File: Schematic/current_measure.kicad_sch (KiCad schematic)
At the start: 14 parts, among them J1 Conn_02x03_Counter_Clockwise, J2 Screw_Terminal_01x02, SW1 SW_Push, U1 STM32G4A1KEUx, U2 LM4040DBZ-2.0, U3 INA186

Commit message: Week 27.10.2025
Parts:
- removed U2: LM4040DBZ-2.0, Package_TO_SOT_SMD:SOT-23, symbol Reference_Voltage:LM4040DBZ-2.0
- removed U3: INA186, Package_TO_SOT_SMD:SOT-23-5_HandSoldering, symbol Amplifier_Current:INA180A1
- added C10: 10n, symbol Device:C
- added C11, C12, C13: 100n, symbol Device:C
- added C14: 1u, symbol Device:C
- added C15: 10u, symbol Device:C
- added C16: 0.1u, symbol Device:C
- added C17, C5: C, symbol Device:C
- added C6, C7: 0.1µ, symbol Device:C
- added C8: 4.7µ, symbol Device:C
- added C9: 10µ, symbol Device:C
- added J3: Conn_01x04_Pin, Connector_PinHeader_2.54mm:PinHeader_1x04_P2.54mm_Vertical, symbol Connector:Conn_01x04_Pin
- added J4: Conn_01x02, Connector_PinHeader_2.54mm:PinHeader_1x02_P2.54mm_Vertical, symbol Connector_Generic:Conn_01x02
- added R10: 220, symbol Device:R
- added R11: 49.9, symbol Device:R
- added R12: 910, symbol Device:R
- added R13: 100, symbol Device:R
- added R14, R7: 10, symbol Device:R
- added R5: 10k, symbol Device:R
- added R6: 1k, symbol Device:R
- added R8: 820k, symbol Device:R
- added R9: 499, symbol Device:R
- added U2: INA186, Package_TO_SOT_SMD:SOT-363_SC-70-6_Handsoldering, symbol Amplifier_Current:INA199xxDCK
- added U3: MCP6001-OT, Package_SO:SOIC-8_3.9x4.9mm_P1.27mm, symbol Amplifier_Operational:MCP6001-OT
- added U4: OPA350, Package_SO:SOIC-8_3.9x4.9mm_P1.27mm, symbol Amplifier_Operational:OPA356xxD
- added U5, U6: 6N137, Package_DIP:DIP-8_W7.62mm, symbol Isolator:6N137
- added U7: MIC5365-3.3YD5, Package_TO_SOT_SMD:TSOT-23-5_HandSoldering, symbol Regulator_Linear:MIC5365-3.3YD5
- C1: value 470n -> 22n
- C2: value C -> 0.1u
- C3: value C -> 4.7u
- C4: value C -> 10u
- R1: value 100 -> 9.1k; footprint Resistor_SMD:R_0805_2012Metric_Pad1.20x1.40mm_HandSolder -> (none)
- R3, R4: value 100 -> 1k
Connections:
- net +3.3V: now also C12.1, C7.1, C8.1, C9.1, U2.3 (V+), U3.2 (V-), U4.7 (V+), U6.8 (VCC), U7.5 (VOUT); no longer R1.1
- net Current_measure: now also C17.1, R14.2, R6.1
- net GND: now also SW1.1, C10.2, C12.2, C13.2, C14.2, C15.2, C16.2, C17.2, C5.2, C6.2, C7.2, C8.2, C9.2, J4.1 (Pin_1), R11.2, R12.2, U2.2 (GND), U3.5 (V+), U4.4 (V-), U6.5 (GND), U7.2 (GND)
- net ~{RESET}: now also SW1.2, C5.1
- net at C1.1, R3.2: now also U2.4 (+)
- net at C1.2, R4.2: now also U2.5 (-)
- net at R1.2: now also R12.1, U3.3 (+)
- new net: R5.2, R7.2, U4.6
- new net: C14.1, C15.1, C16.1, J4.2 (Pin_2), R13.1, U7.1 (VIN)
- new net: C13.1, R13.2, U7.3 (EN)
- new net: R5.1, R6.2, U4.3 (+)
- new net: R11.1, R8.2, R9.2, U4.2 (-)
- new net: R14.1, U2.6
- new net: U2.1 (REF), U3.1, U3.4 (-)
- new net: C10.1, C11.1, R10.2
- new net ADC_in: C6.1, R7.1
- new net DAC_ref_{offset}: R1.1
- new net DAC_{offset}: R9.1
- new net Trig: C11.2, R8.1
- new net Trig_{gen}: R10.1
- new net USB_+5: J3.4 (Pin_4), U5.8 (VCC)
- new net USB_GND: J3.1 (Pin_1), U5.5 (GND), U5.7 (EN), U6.3 (C)
- new net USB_RxD: J3.2 (Pin_2), U5.6 (VO)
- new net USB_TxD: J3.3 (Pin_3), U6.2 (A)
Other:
- note added: "Zależy mi na tym aby nie tłumić sygnału mierzonego!"
- note added: "dla V_{trig} = ±1.024 R_{8}=2.0MΩ dla V_{trig} = ±1.165 R_{8}=3.3MΩ"
- note added: "f_{3dB}=160kHz"
- moved on the sheet: C1, C2, C3, C4, J1, J2, R2, R3, R4, SW1

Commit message: Week 03.11.2025
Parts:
- removed C17: C, symbol Device:C
- removed R11: 49.9, symbol Device:R
- removed R12: 910, symbol Device:R
- added C10, C11, C12: 100n, symbol Device:C
- added C13: 1u, symbol Device:C
- added C14: 4.7u, symbol Device:C
- added R15: 680, symbol Device:R
- added RV1: 200, symbol Device:R_Potentiometer
- added RV2: 4.7k, symbol Device:R_Potentiometer
- added U8: STM32G431C8Tx, Package_QFP:LQFP-48_7x7mm_P0.5mm, symbol MCU_ST_STM32G4:STM32G431C8Tx
- added Y1: 8MHz, Filter:Filter_Mini-Circuits_FV1206-7, symbol Device:Resonator
- C15: renamed from C5; value C -> 100n
- C3: renamed from C16; value 0.1u -> 100n
- R10: renamed from R8; value 820k -> 1.62M
- R11: renamed from R9; value 499 -> 910
- R14: value 10 -> 680
- R5: renamed from R1; value 9.1k -> 30k
- R7: renamed from R5; value 10k -> 100k
- R8: renamed from R6; value 1k -> 10k
- renumbered C15 to C1, C7 to C16, C8 to C17, C9 to C18, C6 to C19, C14 to C2, C11 to C20, C10 to C21, C2 to C4, C3 to C5, C4 to C6, C13 to C7, C1 to C8, C12 to C9, J4 to J1, J3 to J2, J2 to J3, J1 to J4, R13 to R1, R10 to R13, R3 to R2, R2 to R3, R7 to R9, U7 to U1, U5 to U3, U6 to U4, U3 to U5, U1 to U6, U4 to U7
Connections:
- net DAC_ref_{offset} is gone; now on net +3.3V: R5.1
- net +3.3V: now also U6.1 (VDD), U6.15 (VDDA), U6.17 (VDD), C10.1, C11.1, C12.1, C13.1, C14.1
- net Current_measure: now also U2.6; no longer R14.2
- net GND: now also U3.3 (C), U4.7 (EN), U6.14 (VSSA), U6.16 (VSS), U6.32 (VSS), U6.33 (VSS), C10.2, C11.2, C12.2, C13.2, C14.2, RV1.2, RV1.3, RV2.2, RV2.3, Y1.2
- net USB_TxD: now also R14.2; no longer U4.2 (A)
- net at R5.2, U5.3 (+): now also RV2.1
- net at U3.2 (A): now also R15.1
- net at R10.2, R11.2, U7.2 (-): now also RV1.1
- net at R14.1: now also U4.2 (A); no longer U2.6
- net MCU_RxD: now reaches U4.6 (VO)
- net REF_{offset}: now reaches U2.1 (REF), U5.1, U5.4 (-)
- net xTAL_{1}: now reaches U6.2 (PF0)
- net xTAL_{1}: now also Y1.1
- net xTAL_{2}: now reaches U6.3 (PF1)
- net xTAL_{2}: now also Y1.3
- net DAC_{offset} renamed Offset
- new net: U8.23 (VSS), U8.35 (VSS), U8.47 (VSS)
- new net MCU_TxD: R15.2
- no-connect marks 0 -> 4
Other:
- note added: "100"
- note added: "2k"
- moved on the sheet: C1, C15, C16, C17, C18, C19, C2, C20, C21, C3, C4, C5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

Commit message: Update schematic
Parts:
- removed C7: 100n, symbol Device:C
- removed J3: Screw_Terminal_01x02, symbol Connector:Screw_Terminal_01x02
- removed R1: 100, symbol Device:R
- removed RV1: 200, symbol Device:R_Potentiometer
- removed U5: MCP6001-OT, Package_SO:SOIC-8_3.9x4.9mm_P1.27mm, symbol Amplifier_Operational:MCP6001-OT
- removed U6: STM32G4A1KEUx, Package_DFN_QFN:QFN-32-1EP_5x5mm_P0.5mm_EP3.45x3.45mm, symbol MCU_ST_STM32G4:STM32G4A1KEUx
- added C22: 1µ, Capacitor_SMD:C_0805_2012Metric, symbol Device:C
- added C23: 0.1µ, Capacitor_SMD:C_0805_2012Metric, symbol Device:C
- added C6: 100n, Capacitor_SMD:C_0805_2012Metric, symbol Device:C
- added D1, D2: MBR1020VL, Diode_SMD:D_SMA_Handsoldering, symbol Diode:MBR1020VL
- added D3, D4: LED, LED_SMD:LED_0805_2012Metric_Pad1.15x1.40mm_HandSolder, symbol Device:LED
- added J2: Screw_Terminal_01x02, TerminalBlock:TerminalBlock_Xinya_XY308-2.54-2P_1x02_P2.54mm_Horizontal, symbol Connector:Screw_Terminal_01x02
- added J4: PowerSupply select, Connector_PinSocket_2.54mm:PinSocket_1x03_P2.54mm_Vertical, symbol Connector:Conn_01x03_Pin
- added J6: Conn_01x04, Connector_PinHeader_2.54mm:PinHeader_1x04_P2.54mm_Vertical, symbol Connector_Generic:Conn_01x04
- added Q1: Si2319CDS, Package_TO_SOT_SMD:SOT-23, symbol Transistor_FET:Si2319CDS
- added R13, R14: 1k, Resistor_SMD:R_0805_2012Metric, symbol Device:R
- added RV2: 2k, Resistor_SMD:R_0805_2012Metric, symbol Device:R_Potentiometer
- added U4: MCP6002-xSN, Package_SO:SOIC-8_3.9x4.9mm_P1.27mm, symbol Amplifier_Operational:MCP6002-xSN
- C1: renamed from C4; footprint (none) -> Capacitor_SMD:C_0805_2012Metric
- C10: renamed from C13; footprint (none) -> Capacitor_SMD:C_0805_2012Metric
- C11: renamed from C14; footprint (none) -> Capacitor_SMD:C_0805_2012Metric
- C12: renamed from C1; footprint (none) -> Capacitor_SMD:C_0805_2012Metric
- C13: renamed from C2; footprint (none) -> Capacitor_SMD:C_0805_2012Metric
- C14: renamed from C3; footprint (none) -> Capacitor_SMD:C_0805_2012Metric
- C15, C16, C17, C18, C19, C20, C21: footprint (none) -> Capacitor_SMD:C_0805_2012Metric
- C2: renamed from C5; footprint (none) -> Capacitor_SMD:C_0805_2012Metric
- C3: renamed from C6; footprint (none) -> Capacitor_SMD:C_0805_2012Metric
- C4: renamed from C8; footprint (none) -> Capacitor_SMD:C_0805_2012Metric
- C5: renamed from C9; footprint (none) -> Capacitor_SMD:C_0805_2012Metric
- C7: renamed from C10; footprint (none) -> Capacitor_SMD:C_0805_2012Metric
- C8: renamed from C11; footprint (none) -> Capacitor_SMD:C_0805_2012Metric
- C9: renamed from C12; footprint (none) -> Capacitor_SMD:C_0805_2012Metric
- R1: renamed from R15; footprint (none) -> Resistor_SMD:R_0805_2012Metric
- R10, R2, R7, R8, R9: footprint (none) -> Resistor_SMD:R_0805_2012Metric
- R11: value 910 -> 100; footprint (none) -> Resistor_SMD:R_0805_2012Metric
- R12: renamed from R13; footprint (none) -> Resistor_SMD:R_0805_2012Metric
- R3: renamed from R14; footprint (none) -> Resistor_SMD:R_0805_2012Metric
- R4: renamed from R3; footprint (none) -> Resistor_SMD:R_0805_2012Metric
- R5: renamed from R4; footprint (none) -> Resistor_SMD:R_0805_2012Metric
- R6: renamed from R5; value 30k -> 19.1k; footprint (none) -> Resistor_SMD:R_0805_2012Metric
- RV1: renamed from RV2; value 4.7k -> 2k; footprint (none) -> Resistor_SMD:R_0805_2012Metric
- renumbered J2 to J1, J1 to J3, J4 to J5, U3 to U1, U4 to U2, U2 to U3, U1 to U5, U8 to U6
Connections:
- net Offset is gone; now on an unnamed net: R11.1
- net SWD is gone; now on net SWDIO: J5.1 (Pin_1)
- net +3.3V: now also U6.21 (VDDA), U6.24 (VDD), U6.36 (VDD), U6.48 (VDD), C6.1, D2.1 (K), D3.2 (A), J6.4 (Pin_4); no longer J5.6 (Pin_6), R6.1
- net GND: now also J3.2 (Pin_2), R11.2, U6.19 (VSSA), U6.23 (VSS), U6.35 (VSS), U6.47 (VSS), C22.2, C23.2, C6.2, J6.1 (Pin_1), R13.2, R14.2, U4.4 (V-); no longer J3.1 (Pin_1)
- net REF_{offset}: now also U4.1, U4.2 (-)
- net SWCLK: now also U6.38 (PA14)
- net xTAL_{1}: now also U6.5 (PF0)
- net xTAL_{2}: now also U6.6 (PF1)
- net ~{RESET}: now also U6.7 (PG10)
- net at R6.2, RV1.1: now also U4.3 (+)
- net +5V: now reaches C12.1, C13.1, C14.1, U5.1 (VIN)
- net +5V: now also D1.1 (K), J4.3 (Pin_3), Q1.3 (D); no longer J3.2 (Pin_2)
- net at R2.1, R4.1: now also J2.1 (Pin_1)
- net at R4.2, R5.1: now also J2.2 (Pin_2)
- net at U5.3 (EN): now also Q1.2 (S)
- net at R10.2, U7.2 (-): now also RV2.1; no longer R11.2
- net V_{ref}: now reaches U6.20 (VREF+)
- net V_{ref}: now also U4.5 (+)
- net SWDIO: now reaches U6.37 (PA13)
- new net: J4.2 (Pin_2), J5.6 (Pin_6)
- new net: D4.1 (K), R14.1
- new net: C22.1, C23.1, U4.8 (V+)
- new net: D3.1 (K), R13.1
- new net +3.3VP: D2.2 (A), J4.1 (Pin_1), Q1.1 (G)
- new net +5VD: D1.2 (A), J3.1 (Pin_1)
- new net GPIO_LED: D4.2 (A)
- new net MCU_I2C_SCL: J6.2 (Pin_2)
- new net MCU_I2C_SDA: J6.3 (Pin_3)
- new net V_{buf}: R6.1, RV2.2, RV2.3, U4.6 (-), U4.7
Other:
- note added: "1k"
- note added: "910"
- note added: "Blink"
- note added: "Power"
- note removed: "100"
- note removed: "2k"
- moved on the sheet: C1, C10, C11, C12, C13, C14, C15, C16, C17, C18, C19, C2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

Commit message: Clean schematic
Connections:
- net +3.3V: now also C22.1, C23.1, U4.8 (V+)
- net ADC_in: now also U6.14 (PA6)
- net GPIO_LED: now also U6.8 (PA0)
- net MCU_I2C_SCL: now also U6.31 (PA9)
- net MCU_I2C_SDA: now also U6.30 (PA8)
- net MCU_RxD: now also U6.11 (PA3)
- net MCU_TxD: now also U6.10 (PA2)
- net Trig_{gen}: now also U6.13 (PA5)
- no-connect marks 4 -> 11
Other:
- note added: "Bufor napięcia referencyjnego"
- note added: "Filtr sygnału trójkątnego z usunięciem składowej stałej"
- note added: "LED sygnalizujące"
- note added: "Podłączenie miktokontrolera"
- note added: "Podłączenie wyswietlacza"
- note added: "Transmija szeregowa danych z izolacją optyczną"
- note added: "Układ dodający ditherring Ustawienie offsetu na około 1.024 (V_{ref} / 2)"
- note added: "Układ pomiarowy"
- note added: "Zasilanie bufora napięcia referencyjnego"
- note added: "Zasilanie i programowanie układu"
- moved on the sheet: C1, C10, C11, C12, C13, C14, C15, C16, C17, C18, C19, C2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

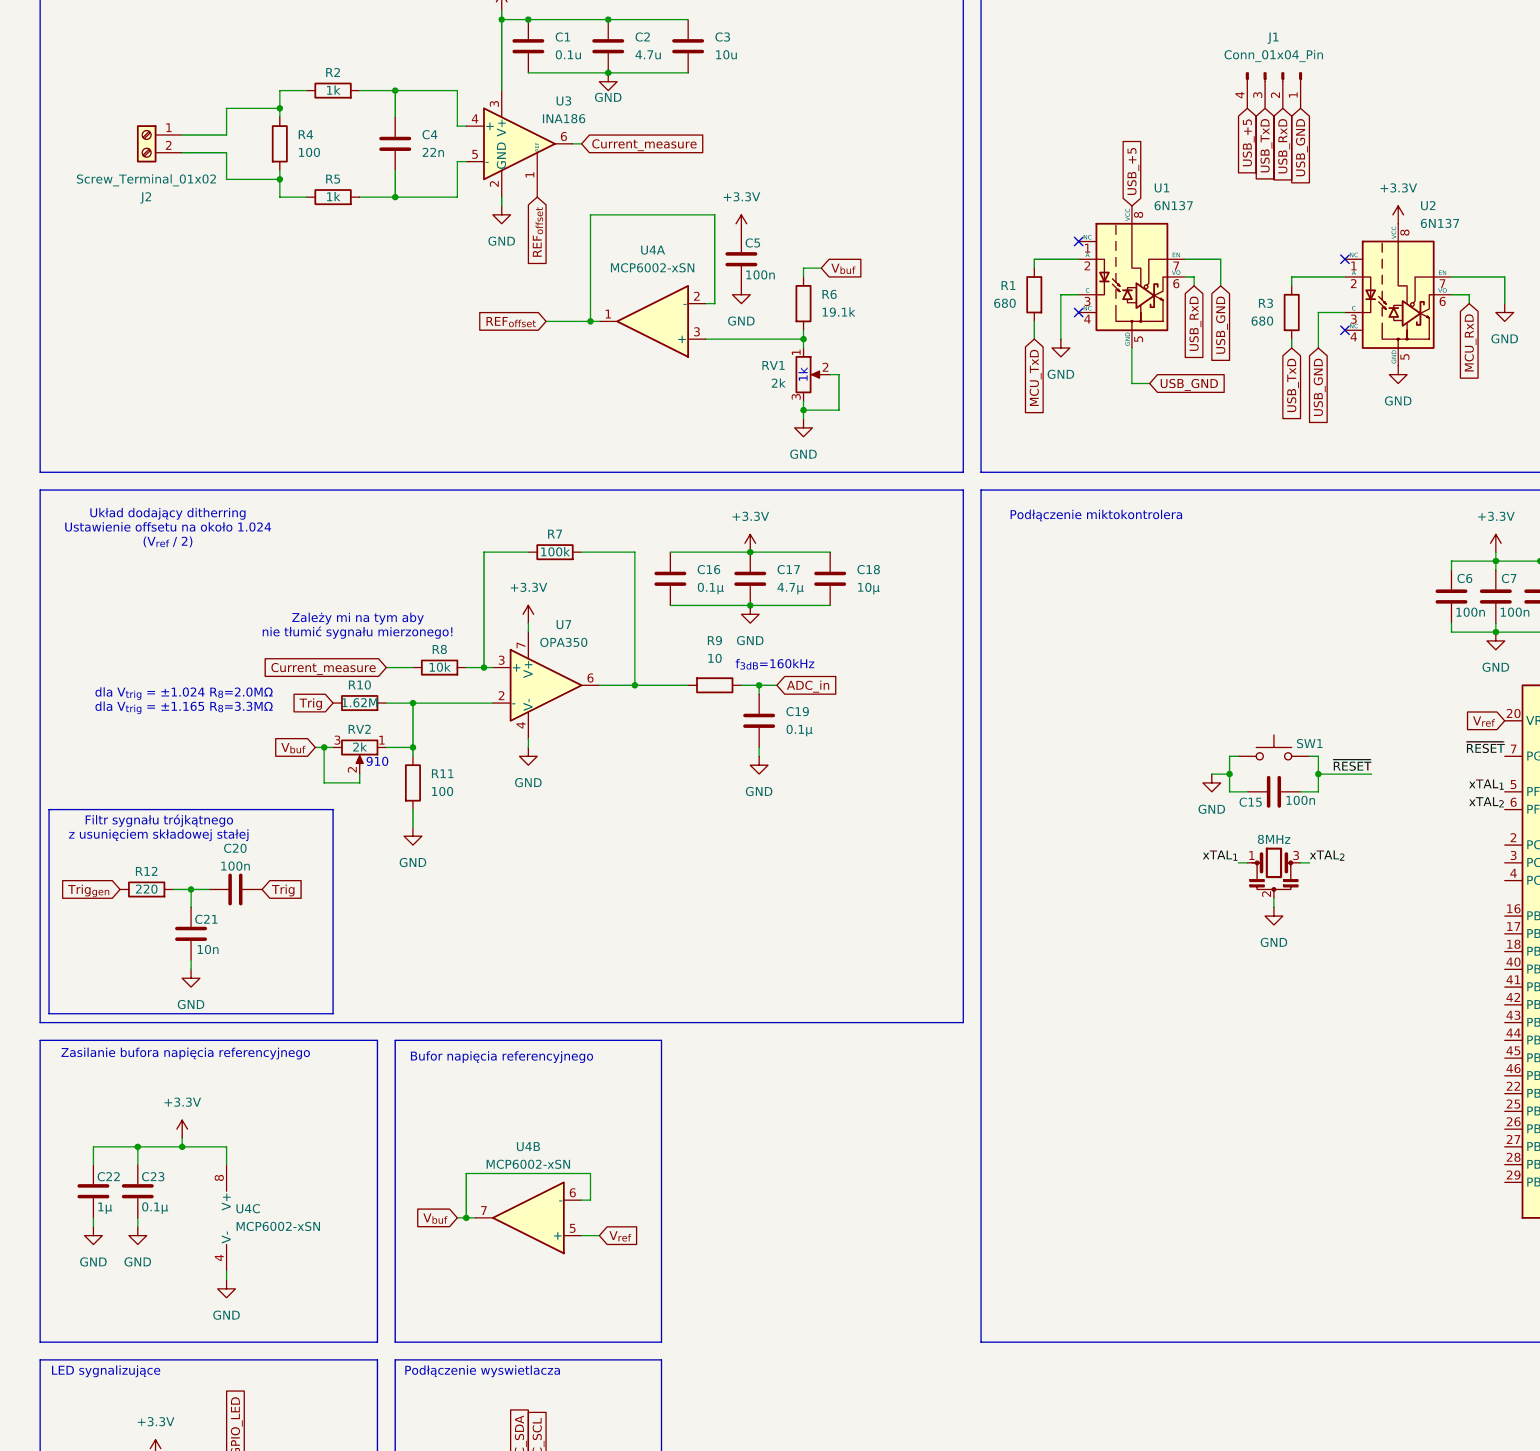
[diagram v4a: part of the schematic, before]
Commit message: Changed buffor amplifiers, changed potentiometer, creating layout
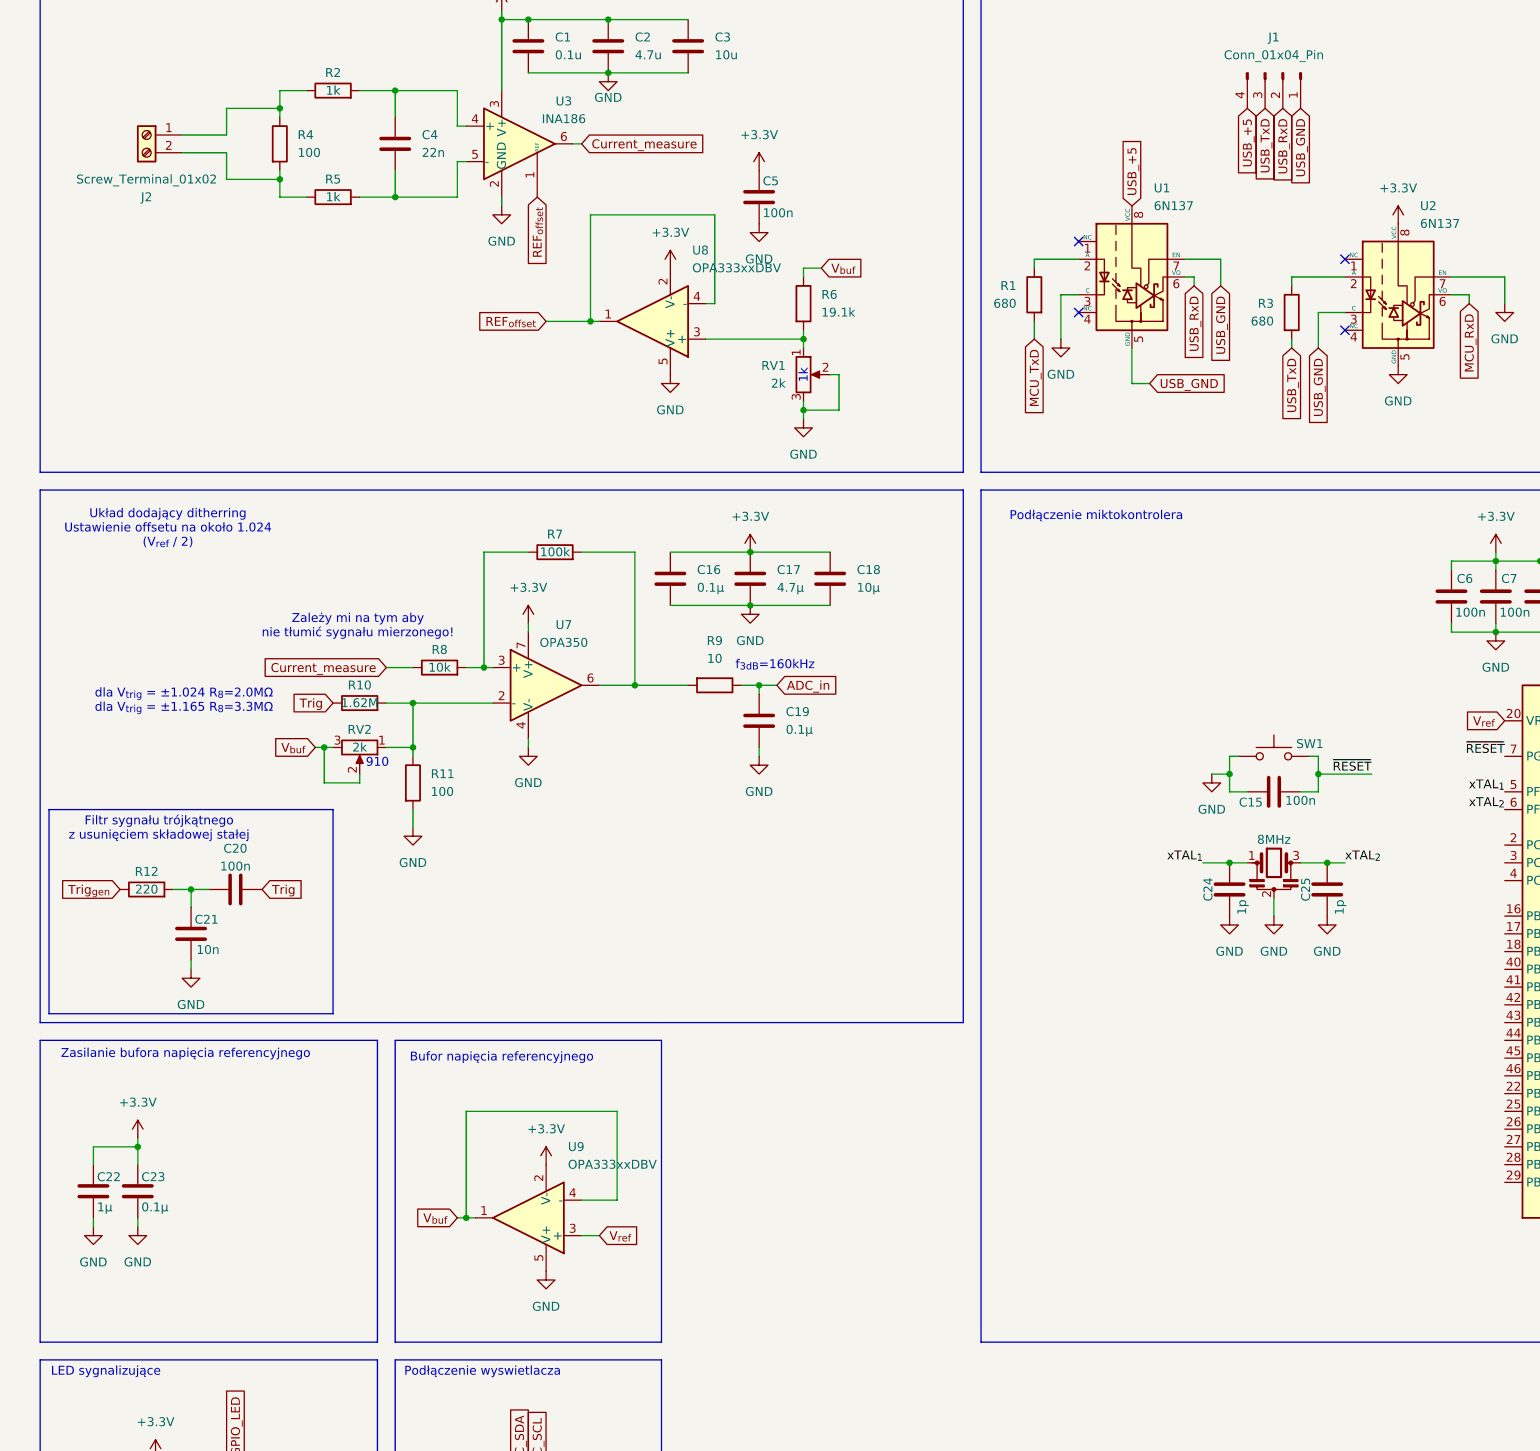
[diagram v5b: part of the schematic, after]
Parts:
- removed U4: MCP6002-xSN, Package_SO:SOIC-8_3.9x4.9mm_P1.27mm, symbol Amplifier_Operational:MCP6002-xSN
- added C24, C25: 1p, Capacitor_SMD:C_0805_2012Metric, symbol Device:C
- added U8, U9: OPA333xxDBV, Package_TO_SOT_SMD:SOT-23-5, symbol Amplifier_Operational:OPA333xxDBV
- RV1, RV2: footprint Resistor_SMD:R_0805_2012Metric -> Potentiometer_THT:Potentiometer_Vishay_T73YP_Vertical
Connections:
- net +3.3V: now also U8.2 (V-), U9.2 (V-)
- net GND: now also C24.2, C25.2, U8.5 (V+), U9.5 (V+)
- net REF_{offset}: now also U8.1, U8.4 (-)
- net V_{buf}: now also U9.1, U9.4 (-)
- net V_{ref}: now also U9.3 (+)
- net xTAL_{1}: now also C24.1
- net xTAL_{2}: now also C25.1
- net at R6.2, RV1.1: now also U8.3 (+)
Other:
- moved on the sheet: C5

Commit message: improved layout
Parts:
- removed C24, C25: 1p, Capacitor_SMD:C_0805_2012Metric, symbol Device:C
